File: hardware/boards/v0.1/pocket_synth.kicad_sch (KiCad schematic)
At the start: 4 parts

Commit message: feat: more DRC cleanup
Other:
- sheet Keypad ports: added VELOCITY_ALERT; removed none
- sheet MCU ports: added VELOCITY_ALERT; removed none
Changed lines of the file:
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@@
+		)
+	)
+	(wire
+		(pts
+			(xy 110.49 93.98) (xy 138.43 93.98)
+		)
+		(stroke
+			(width 0)
+			(type default)
 		)
 	)
@@
 			)
 		)
+		(pin "VELOCITY_ALERT" input
+			(at 110.49 93.98 0)
+			(effects
+				(font
+					(size 1.27 1.27)
+				)
+				(justify right)
+			)
+		)
 		(instances
 			(project "pocket_synth"
@@
 			(effects
 				(font
+					(size 1.27 1.27)
+				)
+				(justify left)
+			)
+		)
+		(pin "VELOCITY_ALERT" output
+			(at 138.43 93.98 180)
+			(effects
+				(font

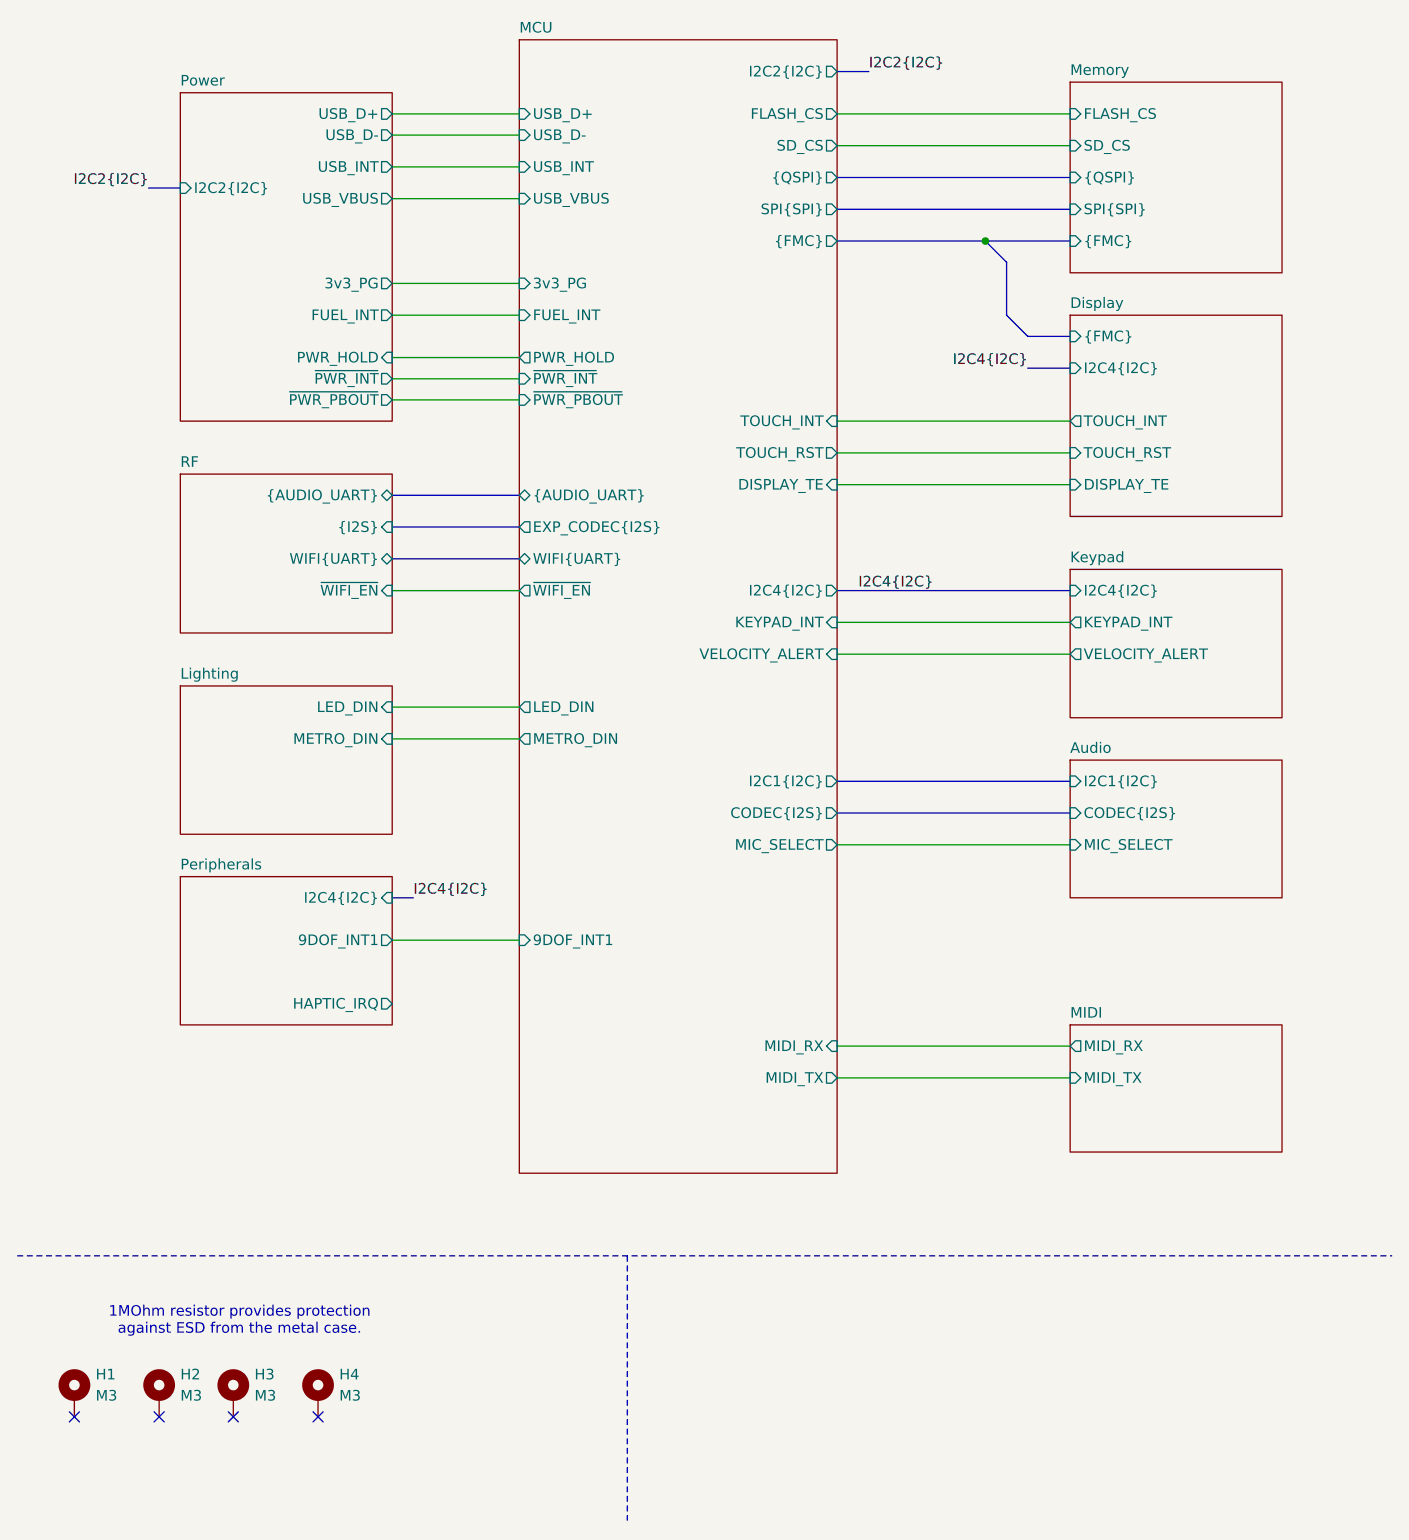
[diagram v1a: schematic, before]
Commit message: feat: add FM reset pins, add fiducials
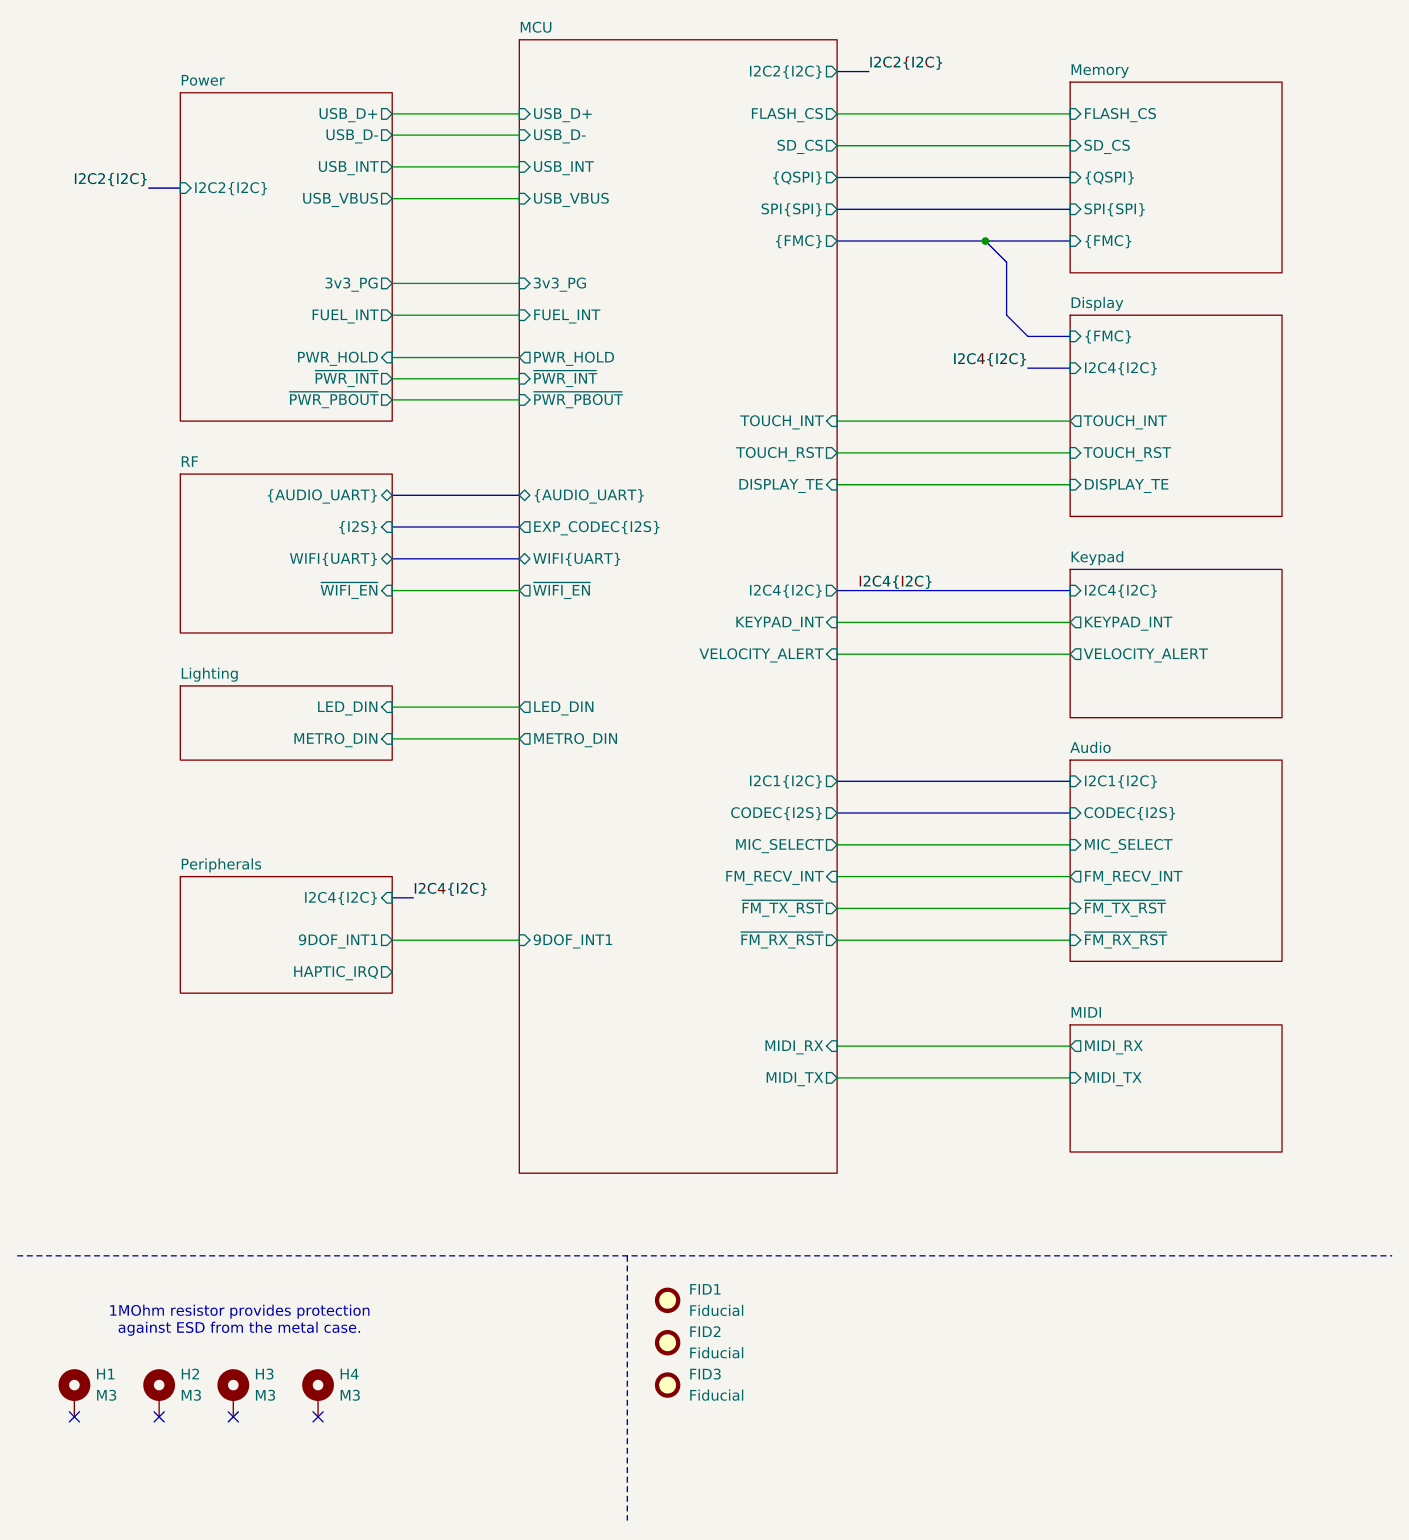
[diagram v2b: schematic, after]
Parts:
- added FID1, FID2, FID3: Fiducial, Fiducial:Fiducial_0.5mm_Mask1.5mm, symbol Mechanical:Fiducial
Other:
- sheet Audio ports: added FM_RECV_INT, ~{FM_RX_RST}, ~{FM_TX_RST}; removed none
- sheet MCU ports: added FM_RECV_INT, ~{FM_RX_RST}, ~{FM_TX_RST}; removed none

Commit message: feat: add display reset connection
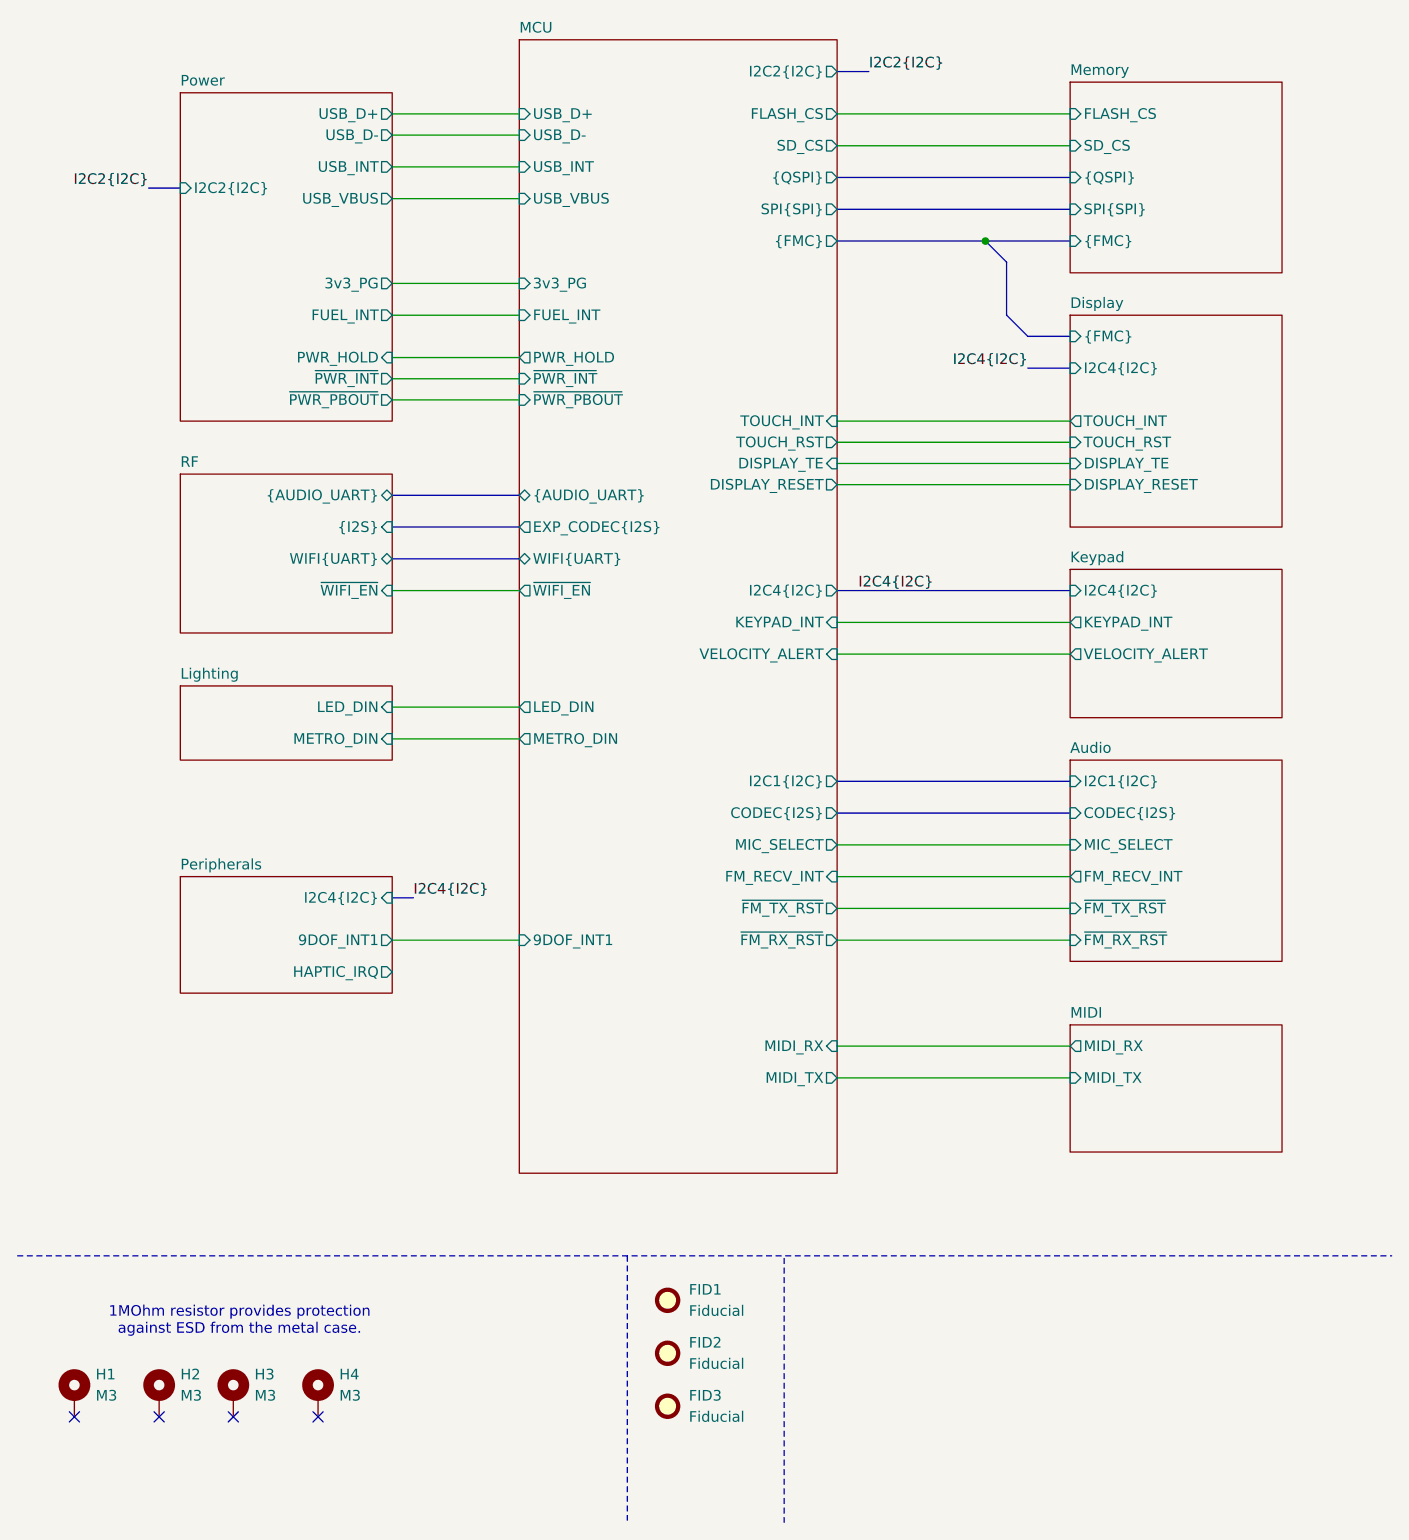
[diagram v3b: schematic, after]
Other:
- sheet Display ports: added DISPLAY_RESET; removed none
- sheet MCU ports: added DISPLAY_RESET; removed none
- moved on the sheet: FID2, FID3
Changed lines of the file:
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@@
 	(wire
 		(pts
+			(xy 110.49 71.12) (xy 138.43 71.12)
+		)
+		(stroke
+			(width 0)
+			(type default)
+		)
+	)
+	(wire
+		(pts
+			(xy 57.15 53.34) (xy 72.39 53.34)
+		)
+		(stroke
+			(width 0)
+			(type default)
+		)
+	)
+	(wire
+		(pts
+			(xy 110.49 90.17) (xy 138.43 90.17)
+		)
+		(stroke
+			(width 0)
+			(type default)
+		)
+	)
+	(bus
+		(pts
+			(xy 128.27 44.45) (xy 138.43 44.45)
+		)
+		(stroke
+			(width 0)
+			(type default)
+		)
+	)
+	(wire
+		(pts
+			(xy 110.49 68.58) (xy 138.43 68.58)
+		)
+		(stroke
+			(width 0)
+			(type default)
+		)
+	)
+	(bus
+		(pts
+			(xy 57.15 74.93) (xy 72.39 74.93)
+		)
+		(stroke
+			(width 0)
+			(type default)
+		)
+	)
+	(bus
+		(pts
+			(xy 110.49 40.64) (xy 138.43 40.64)
+		)
+		(stroke
+			(width 0)
+			(type default)
+		)
+	)
+	(wire
+		(pts
+			(xy 57.15 60.96) (xy 72.39 60.96)
+		)
+		(stroke
+			(width 0)
+			(type default)
+		)
+	)
+	(bus
+		(pts
+			(xy 130.81 46.99) (xy 128.27 44.45)
+		)
+		(stroke
+			(width 0)
+			(type default)
+		)
+	)
+	(wire
+		(pts
+			(xy 110.49 140.97) (xy 138.43 140.97)
+		)
+		(stroke
+			(width 0)
+			(type default)
+		)
+	)
+	(wire
+		(pts
 			(xy 110.49 73.66) (xy 138.43 73.66)
-		)
-		(stroke
-			(width 0)
-			(type default)
-		)
-	)
-	(wire
-		(pts
-			(xy 57.15 53.34) (xy 72.39 53.34)
-		)
-		(stroke
-			(width 0)
-			(type default)
-		)
-	)
-	(wire
-		(pts
-			(xy 110.49 90.17) (xy 138.43 90.17)
-		)
-		(stroke
-			(width 0)
-			(type default)
-		)
-	)
-	(bus
-		(pts
-			(xy 128.27 44.45) (xy 138.43 44.45)
-		)
-		(stroke
-			(width 0)
-			(type default)
-		)
-	)
-	(wire
-		(pts
-			(xy 110.49 69.85) (xy 138.43 69.85)
-		)
-		(stroke
-			(width 0)
-			(type default)
-		)
-	)
-	(bus
-		(pts
-			(xy 57.15 74.93) (xy 72.39 74.93)
-		)
-		(stroke
-			(width 0)
-			(type default)
-		)
-	)
-	(bus
-		(pts
-			(xy 110.49 40.64) (xy 138.43 40.64)
-		)
-		(stroke
-			(width 0)
-			(type default)
-		)
-	)
-	(wire
-		(pts
-			(xy 57.15 60.96) (xy 72.39 60.96)
-		)
-		(stroke
-			(width 0)
-			(type default)
-		)
-	)
-	(bus
-		(pts
-			(xy 130.81 46.99) (xy 128.27 44.45)
-		)
-		(stroke
-			(width 0)
-			(type default)
-		)
-	)
-	(wire
-		(pts
-			(xy 110.49 140.97) (xy 138.43 140.97)
 		)
 		(stroke
@@
 			(width 0)
 			(type default)
+		)
+	)
+	(polyline
+		(pts
+			(xy 104.14 166.37) (xy 104.14 198.12)
+		)
+		(stroke
+			(width 0.127)
+			(type dash)
 		)
 	)
@@
 	(symbol
 		(lib_id "Mechanical:Fiducial")
-		(at 90.17 181.61 0)
+		(at 90.17 184.15 0)
 		(unit 1)
 		(exclude_from_sim no)
@@
 		(fields_autoplaced yes)
 		(property "Reference" "FID3"
-			(at 92.71 180.3399 0)
+			(at 92.71 182.8799 0)
 			(effects
 				(font
@@
 		)
 		(property "Value" "Fiducial"
-			(at 92.71 182.8799 0)
+			(at 92.71 185.4199 0)
 			(effects
 				(font
@@
 		)
 		(property "Footprint" "Fiducial:Fiducial_0.5mm_Mask1.5mm"
-			(at 90.17 181.61 0)
+			(at 90.17 184.15 0)
 			(effects
 				(font
@@
 		)
 		(property "Datasheet" "~"
-			(at 90.17 181.61 0)
+			(at 90.17 184.15 0)
 			(effects
 				(font
@@
 		)
 		(property "Description" "Fiducial Marker"
-			(at 90.17 181.61 0)
+			(at 90.17 184.15 0)
 			(effects
 				(font
@@
 	(symbol
 		(lib_id "Mechanical:Fiducial")
-		(at 90.17 176.53 0)
+		(at 90.17 177.8 0)
 		(unit 1)
 		(exclude_from_sim no)
@@
 		(fields_autoplaced yes)
 		(property "Reference" "FID2"
-			(at 92.71 175.2599 0)
+			(at 92.71 176.5299 0)
 			(effects
 				(font
@@
 		)
 		(property "Value" "Fiducial"
-			(at 92.71 177.7999 0)
+			(at 92.71 179.0699 0)
 			(effects
 				(font
@@
 		)
 		(property "Footprint" "Fiducial:Fiducial_0.5mm_Mask1.5mm"
-			(at 90.17 176.53 0)
+			(at 90.17 177.8 0)
 			(effects
 				(font
@@
 		)
 		(property "Datasheet" "~"
-			(at 90.17 176.53 0)
+			(at 90.17 177.8 0)
 			(effects
 				(font
@@
 		)
 		(property "Description" "Fiducial Marker"
-			(at 90.17 176.53 0)
+			(at 90.17 177.8 0)
 			(effects
 				(font
@@
 		)
 		(pin "TOUCH_RST" output
-			(at 110.49 69.85 0)
+			(at 110.49 68.58 0)
 			(effects
 				(font
@@
 		)
 		(pin "DISPLAY_TE" input
-			(at 110.49 73.66 0)
+			(at 110.49 71.12 0)
 			(effects
 				(font
@@
 		(pin "~{FM_RX_RST}" output
 			(at 110.49 128.27 0)
+			(effects
+				(font
+					(size 1.27 1.27)
+				)
+				(justify right)
+			)
+		)
+		(pin "DISPLAY_RESET" output
+			(at 110.49 73.66 0)
 			(effects
 				(font
@@
 	(sheet
 		(at 138.43 53.34)
-		(size 25.4 24.13)
+		(size 25.4 25.4)
 		(exclude_from_sim no)
 		(in_bom yes)
@@
 		)
 		(property "Sheetfile" "display.kicad_sch"
-			(at 138.43 78.0546 0)
+			(at 138.43 79.3246 0)
 			(effects
 				(font
@@
 		)
 		(pin "DISPLAY_TE" input
-			(at 138.43 73.66 180)
+			(at 138.43 71.12 180)
 			(effects
 				(font
@@
 		)
 		(pin "TOUCH_RST" input
-			(at 138.43 69.85 180)
-			(effects
-				(font
+			(at 138.43 68.58 180)
+			(effects
+				(font
+					(size 1.27 1.27)
+				)
+				(justify left)
+			)
+		)
+		(pin "DISPLAY_RESET" input
+			(at 138.43 73.66 180)
+			(effects
+				(font

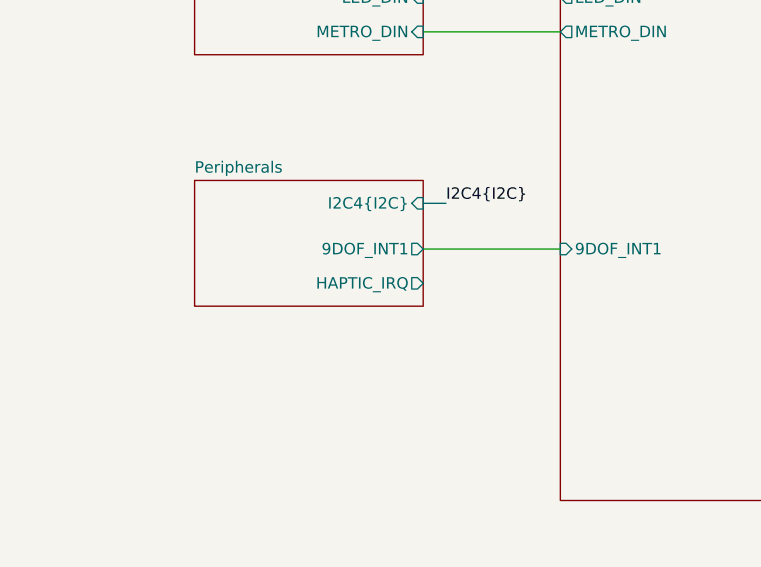
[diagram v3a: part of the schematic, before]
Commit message: chore: make ERC happy
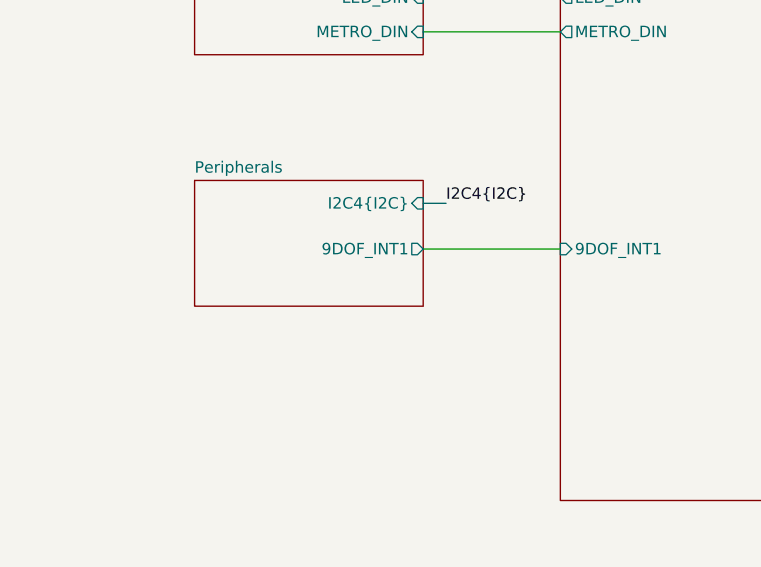
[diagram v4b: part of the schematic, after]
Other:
- sheet Peripherals ports: added none; removed HAPTIC_IRQ
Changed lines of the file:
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@@
-			)
-		)
-		(pin "HAPTIC_IRQ" output
-			(at 57.15 132.08 0)
-			(effects
-				(font
-					(size 1.27 1.27)
-				)
-				(justify right)
 			)
 		)
